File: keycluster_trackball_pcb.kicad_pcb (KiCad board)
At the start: 2 copper layers, 15 x 13.5 mm, 2 parts

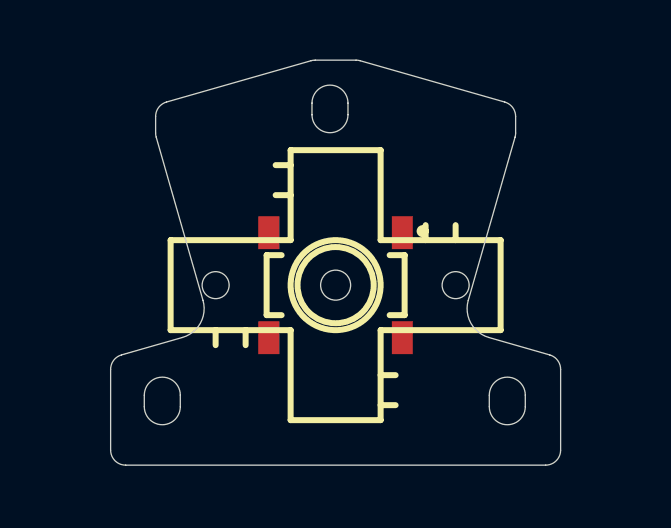
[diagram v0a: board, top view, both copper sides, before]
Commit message: Add version numbers on the silk screen.
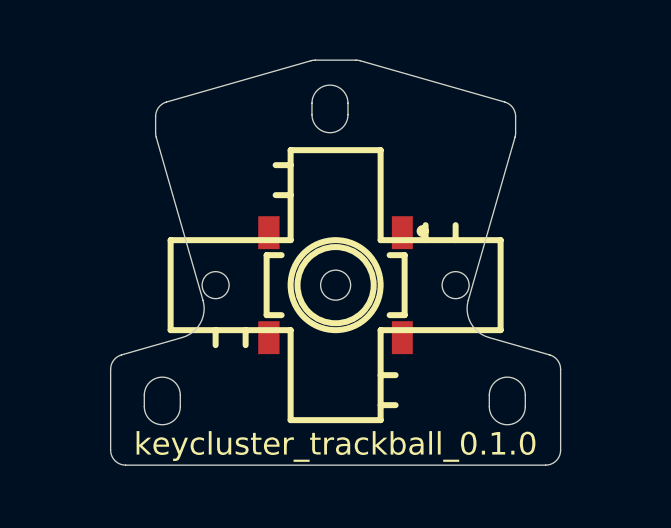
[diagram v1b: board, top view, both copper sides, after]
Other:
- board text added: "keycluster_trackball_0.1.0"
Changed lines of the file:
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@@
-(kicad_pcb (version 20171130) (host pcbnew "(5.0.0)")
+(kicad_pcb (version 20171130) (host pcbnew 5.1.2-f72e74a~84~ubuntu18.04.1)
   (general
     (thickness 1.6)
-    (drawings 37)
+    (drawings 38)
     (tracks 0)
     (zones 0)
@@
     (zone_45_only no)
     (trace_min 0.254)
-    (segment_width 0.2)
-    (edge_width 0.1)
     (via_size 0.889)
     (via_drill 0.635)
@@
     (uvia_min_size 0.508)
     (uvia_min_drill 0.127)
+    (edge_width 0.1)
+    (segment_width 0.2)
     (pcb_text_width 0.3)
     (pcb_text_size 1.5 1.5)
@@
     (pad_to_mask_clearance 0)
     (aux_axis_origin 0 0)
-    (visible_elements 7FFFFFFF)
+    (visible_elements 7FFFEFFF)
     (pcbplotparams
       (layerselection 0x00030_ffffffff)
@@
     (pad 2 smd rect (at 2.225 1.75) (size 0.7 1.1) (layers F.Cu F.Paste F.Mask))
   )
+  (gr_text keycluster_trackball_0.1.0 (at 200 155.3) (layer F.SilkS)
+    (effects (font (size 0.75 0.75) (thickness 0.15)))
+  )
   (gr_circle (center 200 150) (end 200 150.5) (layer Edge.Cuts) (width 0.01))
